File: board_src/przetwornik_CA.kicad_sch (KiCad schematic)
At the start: 4 parts, among them IC5 MCP3202-CI_MS, J23 Conn_01x04, J4 Conn_01x04

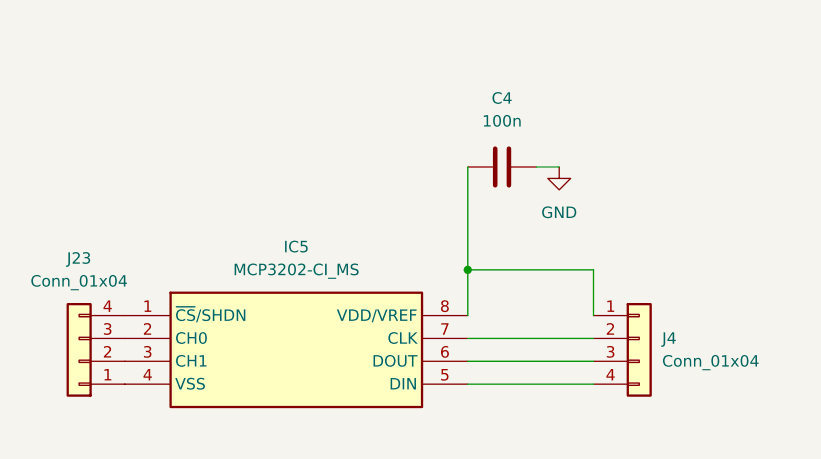
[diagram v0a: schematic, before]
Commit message: Wersja ze sciezkami miedzianymi
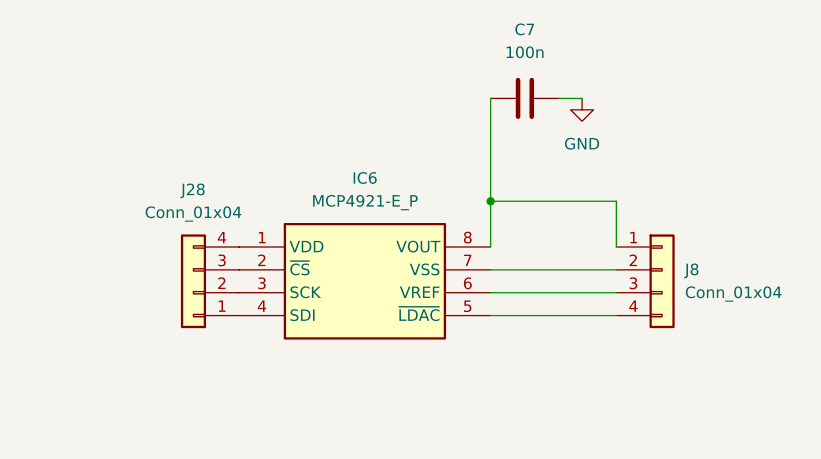
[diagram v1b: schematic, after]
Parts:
- removed C4: 100n, Capacitor_SMD:C_0603_1608Metric, symbol Device:C
- removed IC5: MCP3202-CI_MS, footprints:SOP65P490X110-8N, symbol MCP3202-CI_MS:MCP3202-CI_MS
- removed J23, J4: Conn_01x04, Connector_PinHeader_2.54mm:PinHeader_1x04_P2.54mm_Vertical, symbol Connector_Generic:Conn_01x04
- added C7: 100n, Capacitor_SMD:C_0603_1608Metric, symbol Device:C
- added IC6: MCP4921-E_P, footprints:DIP781W56P254L950H533Q8N, symbol MCP4921-E_P:MCP4921-E_P
- added J28, J8: Conn_01x04, Connector_PinHeader_2.54mm:PinHeader_1x04_P2.54mm_Vertical, symbol Connector_Generic:Conn_01x04
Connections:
- net GND: now also C7.2
- new net: C7.1, IC6.8 (VOUT), J8.1 (Pin_1)
- new net: IC6.4 (SDI), J28.1 (Pin_1)
- new net: IC6.3 (SCK), J28.2 (Pin_2)
- new net: IC6.2 (~{CS}), J28.3 (Pin_3)
- new net: IC6.1 (VDD), J28.4 (Pin_4)
- new net: IC6.7 (VSS), J8.2 (Pin_2)
- new net: IC6.6 (VREF), J8.3 (Pin_3)
- new net: IC6.5 (~{LDAC}), J8.4 (Pin_4)

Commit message: poprawione polaczenia diod i wartosci opornikow, aktualizacja niektorych elementow ze wzgledu na braki w magazynie
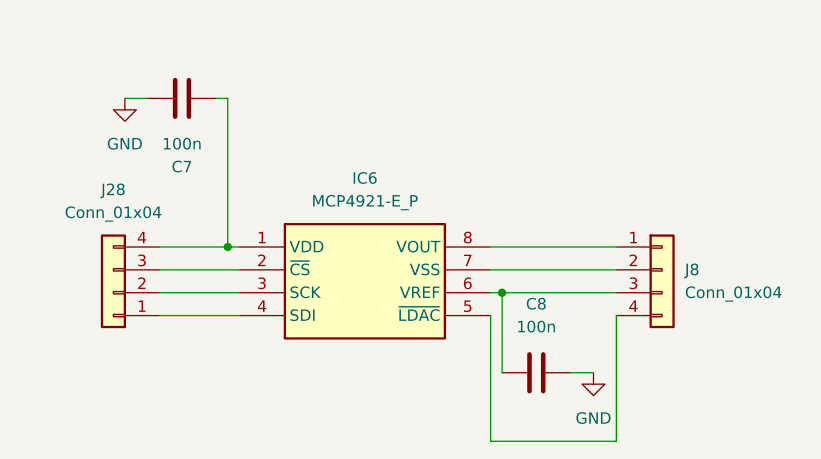
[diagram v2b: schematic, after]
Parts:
- added C8: 100n, Capacitor_SMD:C_0603_1608Metric, symbol Device:C
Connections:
- net GND: now also C8.2
- net at IC6.8 (VOUT), J8.1 (Pin_1): no longer C7.1
- net at IC6.1 (VDD), J28.4 (Pin_4): now also C7.1
- net at IC6.6 (VREF), J8.3 (Pin_3): now also C8.1
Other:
- moved on the sheet: C7, J28

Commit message: Poprawki w schematach. Rozpoczęte korekty płytki
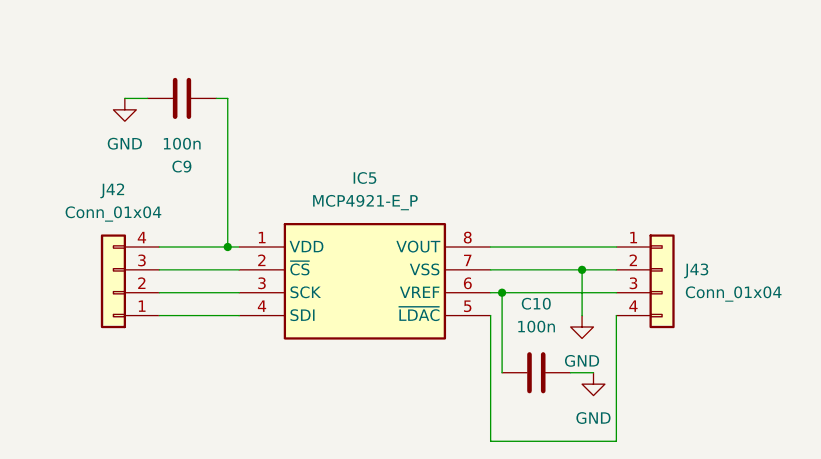
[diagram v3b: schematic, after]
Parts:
- C10: renamed from C8; footprint Capacitor_SMD:C_0603_1608Metric -> Capacitor_SMD:C_0603_1608Metric_Pad1.08x0.95mm_HandSolder
- C9: renamed from C7; footprint Capacitor_SMD:C_0603_1608Metric -> Capacitor_SMD:C_0603_1608Metric_Pad1.08x0.95mm_HandSolder
- IC5: renamed from IC6; footprint footprints:DIP781W56P254L950H533Q8N -> Package_DIP:DIP-8_W7.62mm_Socket_LongPads
- J42: renamed from J28; footprint Connector_PinHeader_2.54mm:PinHeader_1x04_P2.54mm_Vertical -> Connector_PinHeader_2.54mm:PinHeader_1x01_P2.54mm_Vertical
- J43: renamed from J8; footprint Connector_PinHeader_2.54mm:PinHeader_1x04_P2.54mm_Vertical -> Connector_PinHeader_2.54mm:PinHeader_1x01_P2.54mm_Vertical
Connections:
- net GND: now also IC5.7 (VSS), J43.2 (Pin_2)
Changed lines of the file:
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@@
 		(color 0 0 0 0)
 	)
-	(wire
-		(pts
-			(xy 132.08 76.2) (xy 118.11 76.2)
+	(junction
+		(at 128.27 76.2)
+		(diameter 0)
+		(color 0 0 0 0)
+	)
+	(wire
+		(pts
+			(xy 132.08 76.2) (xy 128.27 76.2)
 		)
 		(stroke
@@
 	(wire
 		(pts
+			(xy 128.27 76.2) (xy 128.27 81.28)
+		)
+		(stroke
+			(width 0)
+			(type default)
+		)
+	)
+	(wire
+		(pts
 			(xy 118.11 95.25) (xy 118.11 81.28)
 		)
@@
 	(wire
 		(pts
+			(xy 128.27 76.2) (xy 118.11 76.2)
+		)
+		(stroke
+			(width 0)
+			(type default)
+		)
+	)
+	(wire
+		(pts
 			(xy 132.08 78.74) (xy 119.38 78.74)
 		)
@@
 			(width 0)
 			(type default)
+		)
+	)
+	(symbol
+		(lib_id "power:GND")
+		(at 128.27 81.28 0)
+		(unit 1)
+		(exclude_from_sim no)
+		(in_bom yes)
+		(on_board yes)
+		(dnp no)
+		(fields_autoplaced yes)
+		(property "Reference" "#PWR086"
+			(at 128.27 87.63 0)
+			(effects
+				(font
+					(size 1.27 1.27)
+				)
+				(hide yes)
+			)
+		)
+		(property "Value" "GND"
+			(at 128.27 86.36 0)
+			(effects
+				(font
+					(size 1.27 1.27)
+				)
+			)
+		)
+		(property "Footprint" ""
+			(at 128.27 81.28 0)
+			(effects
+				(font
+					(size 1.27 1.27)
+				)
+				(hide yes)
+			)
+		)
+		(property "Datasheet" ""
+			(at 128.27 81.28 0)
+			(effects
+				(font
+					(size 1.27 1.27)
+				)
+				(hide yes)
+			)
+		)
+		(property "Description" "Power symbol creates a global label with name \"GND\" , ground"
+			(at 128.27 81.28 0)
+			(effects
+				(font
+					(size 1.27 1.27)
+				)
+				(hide yes)
+			)
+		)
+		(pin "1"
+		)
+		(instances
+			(project "board"
+				(path "/772e9f49-cfcf-4cf6-843d-0684684f2d4b/a9412e5b-03b5-4d96-9e57-eaee9dc3e6dc"
+					(reference "#PWR086")
+					(unit 1)
+				)
+			)
 		)
 	)
@@
 		(dnp no)
 		(fields_autoplaced yes)
-		(property "Reference" "C7"
+		(property "Reference" "C9"
 			(at 83.82 64.77 90)
 			(effects
@@
 			)
 		)
-		(property "Footprint" "Capacitor_SMD:C_0603_1608Metric"
+		(property "Footprint" "Capacitor_SMD:C_0603_1608Metric_Pad1.08x0.95mm_HandSolder"
 			(at 80.01 58.1152 0)
 			(effects
@@
 			(project "board"
 				(path "/772e9f49-cfcf-4cf6-843d-0684684f2d4b/a9412e5b-03b5-4d96-9e57-eaee9dc3e6dc"
-					(reference "C7")
+					(reference "C9")
 					(unit 1)
 				)
@@
 		(dnp no)
 		(fields_autoplaced yes)
-		(property "Reference" "#PWR044"
+		(property "Reference" "#PWR084"
 			(at 77.47 63.5 0)
 			(effects
@@
 			(project "board"
 				(path "/772e9f49-cfcf-4cf6-843d-0684684f2d4b/a9412e5b-03b5-4d96-9e57-eaee9dc3e6dc"
-					(reference "#PWR044")
+					(reference "#PWR084")
 					(unit 1)
 				)
@@
 		(dnp no)
 		(fields_autoplaced yes)
-		(property "Reference" "J28"
+		(property "Reference" "J42"
 			(at 76.2 67.31 0)
 			(effects
@@
 			)
 		)
-		(property "Footprint" "Connector_PinHeader_2.54mm:PinHeader_1x04_P2.54mm_Vertical"
+		(property "Footprint" "Connector_PinHeader_2.54mm:PinHeader_1x01_P2.54mm_Vertical"
 			(at 76.2 78.74 0)
 			(effects
@@
 			(project "board"
 				(path "/772e9f49-cfcf-4cf6-843d-0684684f2d4b/a9412e5b-03b5-4d96-9e57-eaee9dc3e6dc"
-					(reference "J28")
+					(reference "J42")
 					(unit 1)
 				)
@@
 		(dnp no)
 		(fields_autoplaced yes)
-		(property "Reference" "J8"
+		(property "Reference" "J43"
 			(at 139.7 76.1999 0)
 			(effects
@@
 			)
 		)
-		(property "Footprint" "Connector_PinHeader_2.54mm:PinHeader_1x04_P2.54mm_Vertical"
+		(property "Footprint" "Connector_PinHeader_2.54mm:PinHeader_1x01_P2.54mm_Vertical"
 			(at 137.16 76.2 0)
 			(effects
@@
 			(project "board"
 				(path "/772e9f49-cfcf-4cf6-843d-0684684f2d4b/a9412e5b-03b5-4d96-9e57-eaee9dc3e6dc"
-					(reference "J8")
+					(reference "J43")
 					(unit 1)
 				)
@@
 		(dnp no)
 		(fields_autoplaced yes)
-		(property "Reference" "#PWR071"
+		(property "Reference" "#PWR087"
 			(at 129.54 93.98 0)
 			(effects
@@
 			(project "board"
 				(path "/772e9f49-cfcf-4cf6-843d-0684684f2d4b/a9412e5b-03b5-4d96-9e57-eaee9dc3e6dc"
-					(reference "#PWR071")
+					(reference "#PWR087")
 					(unit 1)
 				)
@@
 		(dnp no)
 		(fields_autoplaced yes)
-		(property "Reference" "C8"
+		(property "Reference" "C10"
 			(at 123.19 80.01 90)
 			(effects
@@
 			)
 		)
-		(property "Footprint" "Capacitor_SMD:C_0603_1608Metric"
+		(property "Footprint" "Capacitor_SMD:C_0603_1608Metric_Pad1.08x0.95mm_HandSolder"
 			(at 127 86.6648 0)
 			(effects
@@
 			(project "board"
 				(path "/772e9f49-cfcf-4cf6-843d-0684684f2d4b/a9412e5b-03b5-4d96-9e57-eaee9dc3e6dc"
-					(reference "C8")
+					(reference "C10")
 					(unit 1)
 				)
@@
 		(dnp no)
 		(fields_autoplaced yes)
-		(property "Reference" "IC6"
+		(property "Reference" "IC5"
 			(at 104.14 66.04 0)
 			(effects
@@
 			)
 		)
-		(property "Footprint" "footprints:DIP781W56P254L950H533Q8N"
+		(property "Footprint" "Package_DIP:DIP-8_W7.62mm_Socket_LongPads"
 			(at 114.3 168.58 0)
 			(effects
@@
 			(project ""
 				(path "/772e9f49-cfcf-4cf6-843d-0684684f2d4b/a9412e5b-03b5-4d96-9e57-eaee9dc3e6dc"
-					(reference "IC6")
+					(reference "IC5")
 					(unit 1)
 				)

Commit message: Naniesione poprawki na projekcie płytki. Wersja końcowa
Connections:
- net at C9.1, IC5.1 (VDD): now also J42.1 (Pin_1); no longer J42.4 (Pin_4)
- net at IC5.4 (SDI): now also J42.4 (Pin_4); no longer J42.1 (Pin_1)
- net at J42.2 (Pin_2): now also IC5.2 (~{CS}); no longer IC5.3 (SCK)
- net at J42.3 (Pin_3): now also IC5.3 (SCK); no longer IC5.2 (~{CS})
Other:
- moved on the sheet: J42
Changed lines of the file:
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@@
 	(symbol
 		(lib_id "Connector_Generic:Conn_01x04")
-		(at 76.2 78.74 180)
+		(at 76.2 76.2 0)
+		(mirror y)
 		(unit 1)
 		(exclude_from_sim no)
@@
 		(on_board yes)
 		(dnp no)
-		(fields_autoplaced yes)
 		(property "Reference" "J42"
-			(at 76.2 67.31 0)
+			(at 72.136 68.326 0)
 			(effects
 				(font
@@
 		)
 		(property "Value" "Conn_01x04"
-			(at 76.2 69.85 0)
+			(at 72.136 70.358 0)
 			(effects
 				(font
@@
 		)
 		(property "Footprint" "Connector_PinHeader_2.54mm:PinHeader_1x01_P2.54mm_Vertical"
-			(at 76.2 78.74 0)
+			(at 76.2 76.2 0)
 			(effects
 				(font
@@
 		)
 		(property "Datasheet" "~"
-			(at 76.2 78.74 0)
+			(at 76.2 76.2 0)
 			(effects
 				(font
@@
 		)
 		(property "Description" "Generic connector, single row, 01x04, script generated (kicad-library-utils/schlib/autogen/connector/)"
-			(at 76.2 78.74 0)
+			(at 76.2 76.2 0)
 			(effects
 				(font

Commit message: Wprowadzono usprawnienia i poprawki. Wersja ostateczna, wysłana do JLCPCB.
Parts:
- J42, J43: footprint Connector_PinHeader_2.54mm:PinHeader_1x01_P2.54mm_Vertical -> Connector_PinHeader_2.54mm:PinHeader_1x04_P2.54mm_Vertical
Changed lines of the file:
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@@
 			)
 		)
-		(property "Footprint" "Connector_PinHeader_2.54mm:PinHeader_1x01_P2.54mm_Vertical"
+		(property "Footprint" "Connector_PinHeader_2.54mm:PinHeader_1x04_P2.54mm_Vertical"
 			(at 76.2 76.2 0)
 			(effects
@@
 			)
 		)
-		(property "Footprint" "Connector_PinHeader_2.54mm:PinHeader_1x01_P2.54mm_Vertical"
+		(property "Footprint" "Connector_PinHeader_2.54mm:PinHeader_1x04_P2.54mm_Vertical"
 			(at 137.16 76.2 0)
 			(effects
